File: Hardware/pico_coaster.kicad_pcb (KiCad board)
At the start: 2 copper layers, 90 x 90 mm, 142 parts, among them J3 Conn_02x06_Odd_Even, J4 Conn_01x04, J5 USB_C_Receptacle_USB2.0, SW1 SW_Push, SW2 SW_Push, SW3 SW_Push, SW4 SW_Push, SW5 SW_Push, SW6 SW_Push, U1 NCP1117-3.3_SOT223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

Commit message: Swap Boot/Run buttons for pin headers
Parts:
- removed SW1, SW6: SW_Push, Button_Switch_THT:SW_PUSH_6mm_H4.3mm
- added J1: Conn_01x02, Connector_PinHeader_2.54mm:PinHeader_1x02_P2.54mm_Horizontal, B.Cu at (243.7, 92.1)
- added J2: Conn_01x02, Connector_PinHeader_2.54mm:PinHeader_1x02_P2.54mm_Horizontal, B.Cu at (244.0, 71.4)
- moved R6 69.4 mm to (238.9, 71.4)
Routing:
- net Pico_Run: track 8.97 -> 64.8 mm, vias 0 -> 1
- net GND: track 1208.9 -> 1218.4 mm
- net QSPI_SS: track 93.2 -> 99.9 mm, vias 1 -> 2
- net Net-(D21-Pad2): track 92.3 -> 97.1 mm
- net Net-(J2-Pad1): track 0.00 -> 3.70 mm
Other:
- board text added: "3V3"
- board text added: "BOOT"
- board text added: "GND"
- board text added: "RUN"
- board text added: "SWCLK"
- board text added: "SWDIO"

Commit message: fix missing 3v3 connection
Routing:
- net +3V3: track 967.3 -> 968.9 mm
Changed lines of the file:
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@@
     (thickness 1.6)
     (drawings 42)
-    (tracks 1586)
+    (tracks 1589)
     (zones 0)
     (modules 142)
@@
   (segment (start 167.05 90.5) (end 167.275 90.725) (width 0.25) (layer F.Cu) (net 2))
   (segment (start 181.55 78.3) (end 181.45 78.4) (width 0.25) (layer F.Cu) (net 2))
-  (segment (start 181.55 77.15) (end 215.55 77.15) (width 0.25) (layer F.Cu) (net 2))
   (segment (start 181.55 74.95) (end 181.55 77.15) (width 0.25) (layer F.Cu) (net 2))
   (segment (start 181.55 77.15) (end 181.55 78.3) (width 0.25) (layer F.Cu) (net 2))
@@
   (segment (start 215.750001 76.949999) (end 215.55 77.15) (width 0.3) (layer B.Cu) (net 2))
   (segment (start 215.750001 64.149999) (end 215.750001 76.949999) (width 0.3) (layer B.Cu) (net 2))
+  (segment (start 207.55 78.25) (end 206.45 77.15) (width 0.15) (layer F.Cu) (net 2))
+  (segment (start 207.55 78.3) (end 207.55 78.25) (width 0.15) (layer F.Cu) (net 2))
+  (segment (start 206.45 77.15) (end 215.55 77.15) (width 0.25) (layer F.Cu) (net 2))
+  (segment (start 181.55 77.15) (end 206.45 77.15) (width 0.25) (layer F.Cu) (net 2))
   (segment (start 205.941757 62.854944) (end 205.906415 62.854944) (width 0.15) (layer F.Cu) (net 3))
   (segment (start 206.6 63.513187) (end 205.941757 62.854944) (width 0.15) (layer F.Cu) (net 3))

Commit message: add front gnd fill zone and logo on front
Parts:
- added G***: LOGO, jjh:j2h_small, F.Cu at (204.5, 112.7)
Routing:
- net GND: track 1218.4 -> 1232.6 mm, vias 33 -> 46
- added copper zone on F.Cu, net GND
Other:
- board text added: "@JamesjHorton jjhorton.co.uk"

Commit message: Fix DRC errors
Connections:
- net GPIO_10 renamed Net-(U3-Pad13)
- net GPIO_12 renamed Net-(U3-Pad15)
- net GPIO_13 renamed Net-(U3-Pad16)
- net GPIO_14 renamed Net-(U3-Pad17)
- net GPIO_15 renamed Net-(U3-Pad18)
- net GPIO_16 renamed Net-(U3-Pad27)
- net GPIO_17 renamed Net-(U3-Pad28)
- net GPIO_18 renamed Net-(U3-Pad29)
- net GPIO_19 renamed Net-(U3-Pad30)
- net GPIO_20 renamed Net-(U3-Pad31)
- net GPIO_21 renamed Net-(U3-Pad32)
- net GPIO_22 renamed Net-(U3-Pad34)
- net GPIO_23 renamed Net-(U3-Pad35)
- net GPIO_24 renamed Net-(U3-Pad36)
- net GPIO_8 renamed Net-(U3-Pad11)
- net GPIO_9 renamed Net-(U3-Pad12)
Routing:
- net +3V3: track 968.9 -> 977.0 mm, vias 11 -> 13
- net QSPI_SS: track 99.9 -> 102.0 mm
- net GND: vias 46 -> 47

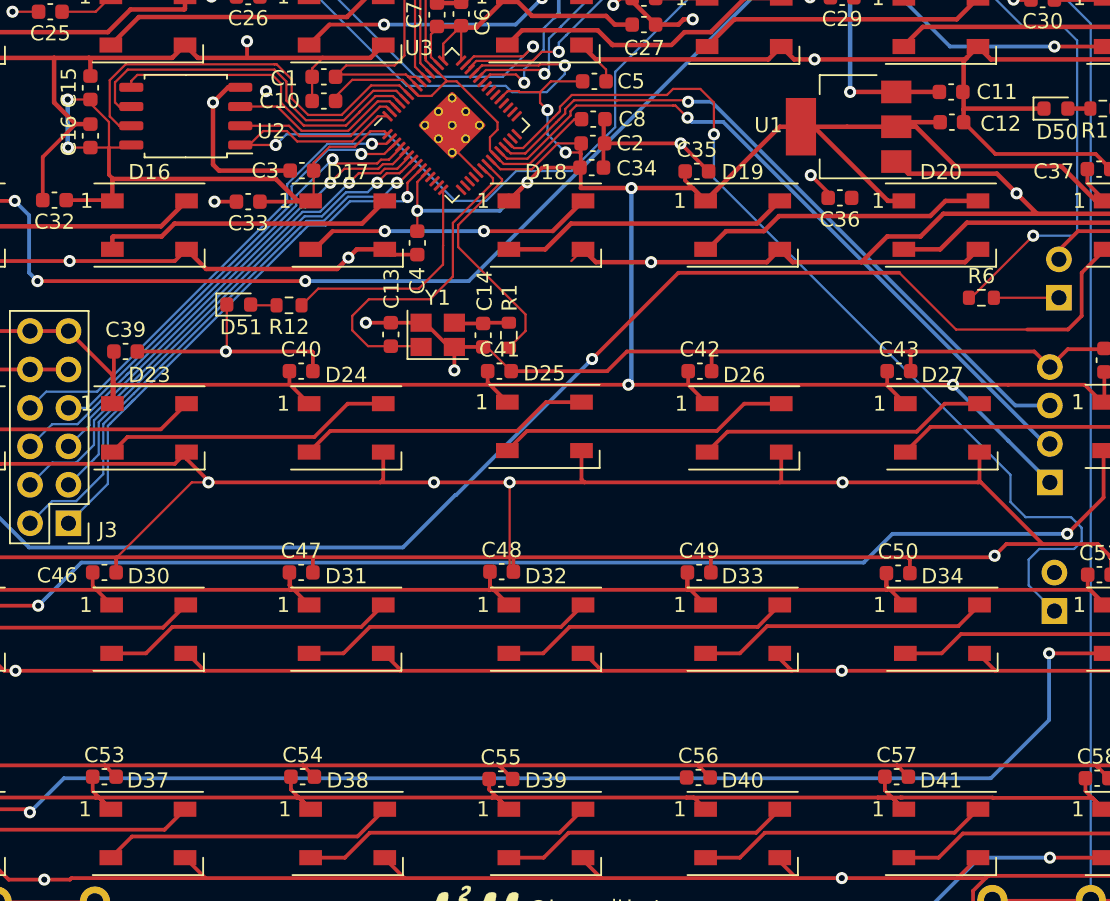
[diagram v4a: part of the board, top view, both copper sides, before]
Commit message: fix unconnected DRC errors
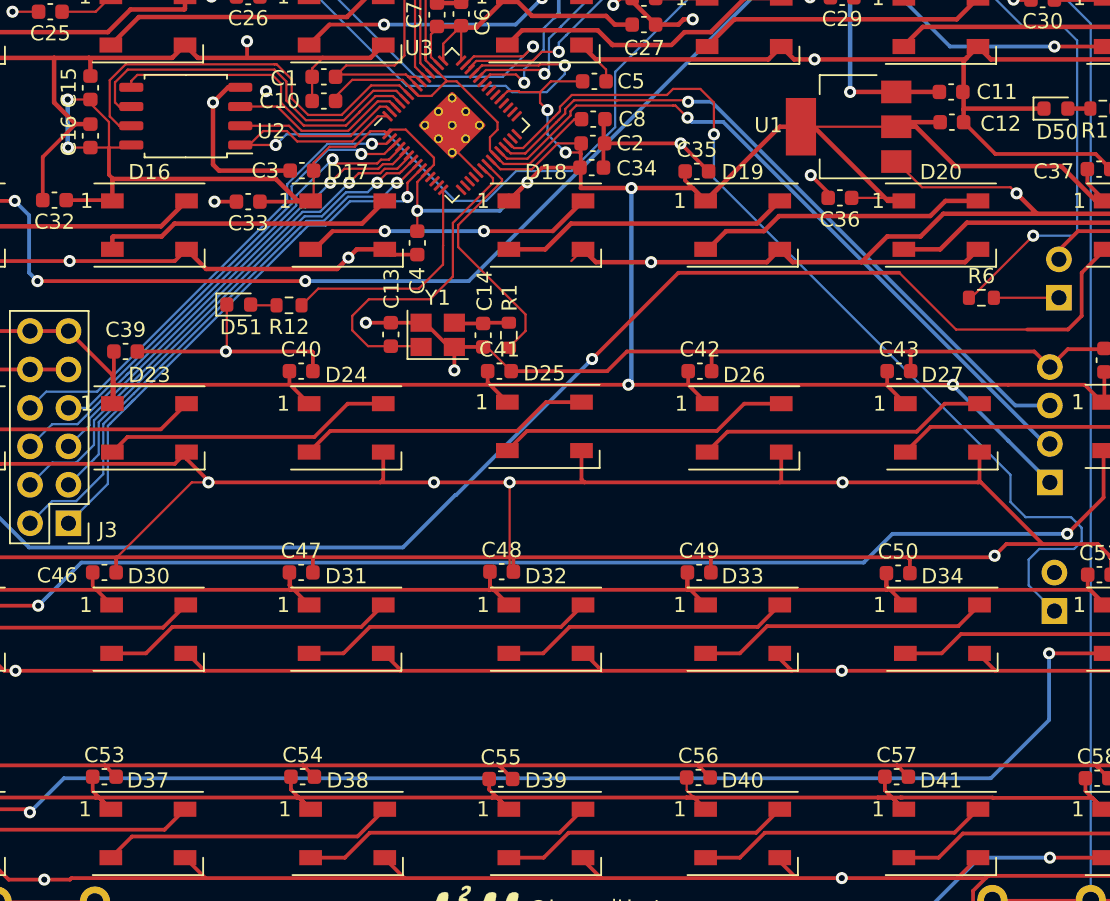
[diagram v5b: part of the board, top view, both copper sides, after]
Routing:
- net +3V3: track 977.0 -> 988.4 mm
- net VBUS: track 52.3 -> 55.4 mm
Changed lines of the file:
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@@
     (thickness 1.6)
     (drawings 43)
-    (tracks 1633)
+    (tracks 1644)
     (zones 0)
     (modules 143)
@@
   (segment (start 249.780003 64.149999) (end 248.080001 65.850001) (width 0.3) (layer F.Cu) (net 1))
   (segment (start 251.95 68.2) (end 253.050001 67.099999) (width 0.3) (layer F.Cu) (net 1))
-  (segment (start 234.05001 63.20001) (end 239.900008 63.20001) (width 0.3) (layer F.Cu) (net 1))
-  (segment (start 233.25 62.4) (end 234.05001 63.20001) (width 0.3) (layer F.Cu) (net 1))
-  (segment (start 239.900008 63.20001) (end 241.199999 64.500001) (width 0.3) (layer F.Cu) (net 1))
   (segment (start 242.549999 65.850001) (end 236.357119 65.850001) (width 0.3) (layer F.Cu) (net 1))
   (segment (start 248.080001 65.850001) (end 242.549999 65.850001) (width 0.3) (layer F.Cu) (net 1))
@@
   (via (at 187.8 83.6) (size 0.8) (drill 0.4) (layers F.Cu B.Cu) (net 1))
   (via (at 191.6 57.75) (size 0.8) (drill 0.4) (layers F.Cu B.Cu) (net 1))
+  (segment (start 240.8 64.100002) (end 241.199999 64.500001) (width 0.15) (layer F.Cu) (net 1))
+  (segment (start 234.950002 64.100002) (end 240.8 64.100002) (width 0.15) (layer F.Cu) (net 1))
+  (segment (start 233.25 62.4) (end 234.950002 64.100002) (width 0.15) (layer F.Cu) (net 1))
   (segment (start 168.25 38.2) (end 168.25 38.15) (width 0.3) (layer F.Cu) (net 2))
   (segment (start 168.25 38.15) (end 169.8 36.6) (width 0.3) (layer F.Cu) (net 2))
@@
   (segment (start 244.14 62.7) (end 246.44 65) (width 0.3) (layer F.Cu) (net 2))
   (segment (start 233.25 60.1) (end 234.55 60.1) (width 0.3) (layer F.Cu) (net 2))
-  (segment (start 233.25 60.1) (end 230 60.1) (width 0.3) (layer F.Cu) (net 2))
-  (segment (start 230 60.1) (end 226.95 60.1) (width 0.3) (layer F.Cu) (net 2))
   (segment (start 227.8 60.1) (end 226.95 60.1) (width 0.3) (layer F.Cu) (net 2))
   (segment (start 232.7 65) (end 227.8 60.1) (width 0.3) (layer F.Cu) (net 2))
@@
   (segment (start 193.15 90.4) (end 194.45 91.7) (width 0.25) (layer F.Cu) (net 2))
   (segment (start 193.15 89.55) (end 193.15 90.4) (width 0.25) (layer F.Cu) (net 2))
-  (segment (start 180.15 90.45) (end 181.4 91.7) (width 0.25) (layer F.Cu) (net 2))
   (segment (start 180.15 89.55) (end 180.15 90.45) (width 0.25) (layer F.Cu) (net 2))
   (segment (start 167.05 89.65) (end 167.05 90.5) (width 0.25) (layer F.Cu) (net 2))
@@
   (segment (start 204.5 55.7) (end 204.5 53.425) (width 0.15) (layer F.Cu) (net 2))
   (segment (start 204.492202 55.707798) (end 204.5 55.7) (width 0.15) (layer F.Cu) (net 2))
+  (segment (start 226.95 60.1) (end 233.25 60.1) (width 0.15) (layer F.Cu) (net 2))
+  (segment (start 233.55 64.8) (end 233.75 65) (width 0.15) (layer F.Cu) (net 2))
+  (segment (start 230.3 64.8) (end 233.55 64.8) (width 0.15) (layer F.Cu) (net 2))
+  (segment (start 219.4 103.95) (end 220.65 105.2) (width 0.15) (layer F.Cu) (net 2))
+  (segment (start 219.4 103.1) (end 219.4 103.95) (width 0.15) (layer F.Cu) (net 2))
+  (segment (start 180.15 90.45) (end 180.4 90.7) (width 0.15) (layer F.Cu) (net 2))
+  (segment (start 180.4 90.7) (end 181.4 91.7) (width 0.25) (layer F.Cu) (net 2))
+  (segment (start 199.790949 60.290676) (end 200.840676 60.290676) (width 0.15) (layer F.Cu) (net 2))
+  (segment (start 199.630843 60.450782) (end 199.790949 60.290676) (width 0.15) (layer F.Cu) (net 2))
+  (segment (start 199.630843 60.592202) (end 199.630843 60.450782) (width 0.15) (layer F.Cu) (net 2))
+  (segment (start 200.840676 60.290676) (end 202.7 62.15) (width 0.15) (layer F.Cu) (net 2))
+  (segment (start 202.7 62.614213) (end 202.176427 63.137786) (width 0.15) (layer F.Cu) (net 2))
+  (segment (start 202.7 62.15) (end 202.7 62.614213) (width 0.15) (layer F.Cu) (net 2))
   (segment (start 205.941757 62.854944) (end 205.906415 62.854944) (width 0.15) (layer F.Cu) (net 3))
   (segment (start 206.6 63.513187) (end 205.941757 62.854944) (width 0.15) (layer F.Cu) (net 3))
@@
   (segment (start 229.9 49.2) (end 212.8 49.2) (width 0.3) (layer F.Cu) (net 14))
   (segment (start 233.25 57.8) (end 236.1 57.8) (width 0.3) (layer F.Cu) (net 14))
+  (segment (start 233.25 57.8) (end 230.2 57.8) (width 0.15) (layer F.Cu) (net 14))
   (segment (start 195.05 70.8) (end 193.95 71.9) (width 0.15) (layer F.Cu) (net 15))
   (segment (start 203.3 69.2) (end 201.7 70.8) (width 0.15) (layer F.Cu) (net 15))

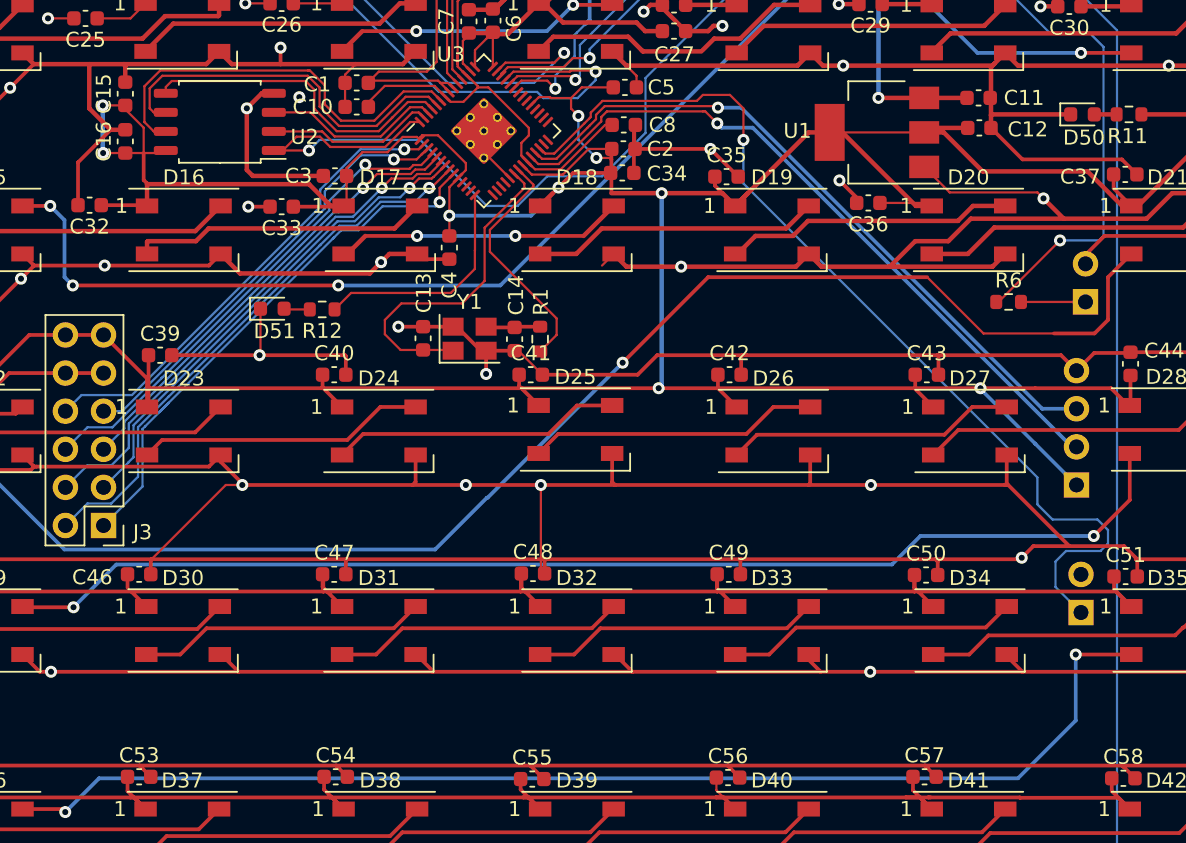
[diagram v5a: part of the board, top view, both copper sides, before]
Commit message: Add 2.54mm power in connector
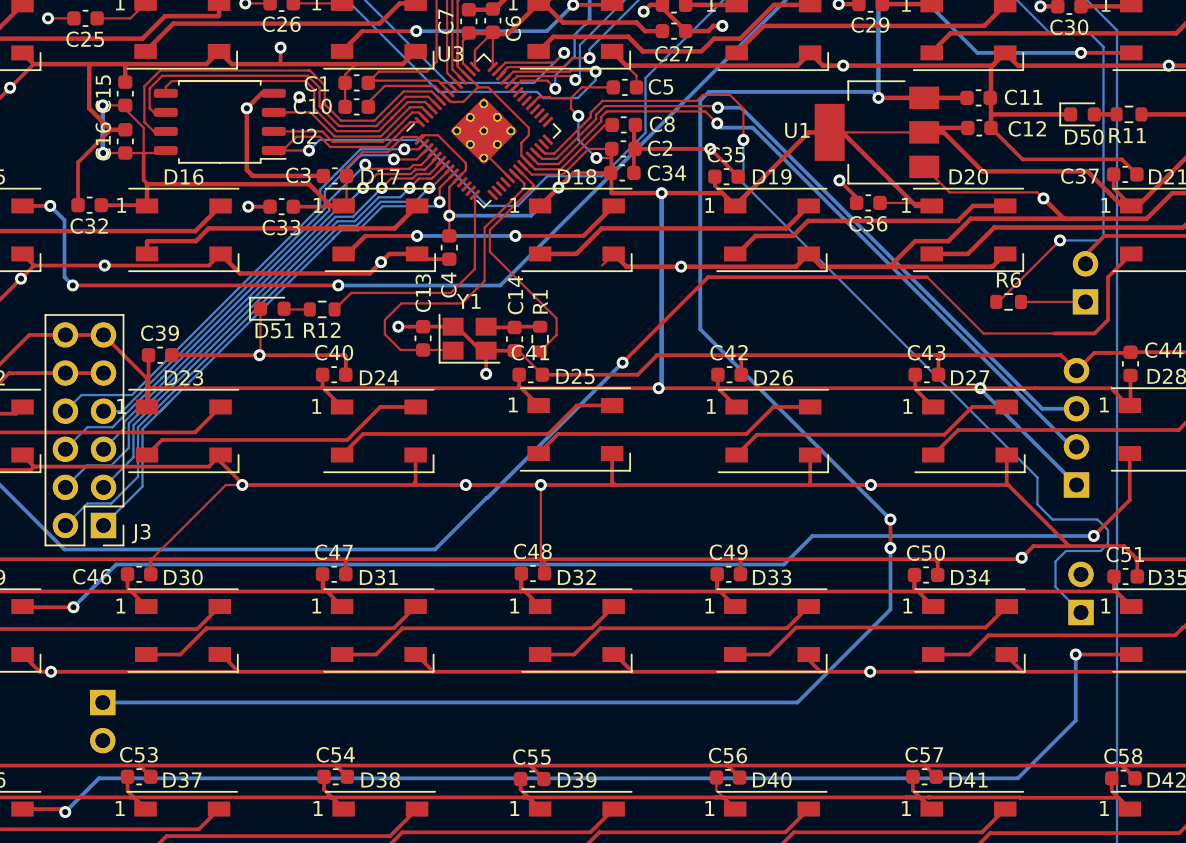
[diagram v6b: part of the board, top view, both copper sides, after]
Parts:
- added J6: Conn_01x02, Connector_PinHeader_2.54mm:PinHeader_1x02_P2.54mm_Horizontal, B.Cu at (178.5, 98.1)
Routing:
- net VBUS: track 55.4 -> 161.9 mm, vias 2 -> 4
